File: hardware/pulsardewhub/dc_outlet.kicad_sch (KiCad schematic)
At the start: 18 parts, among them J101 5A DC / center +, U101 TPS26631PWP

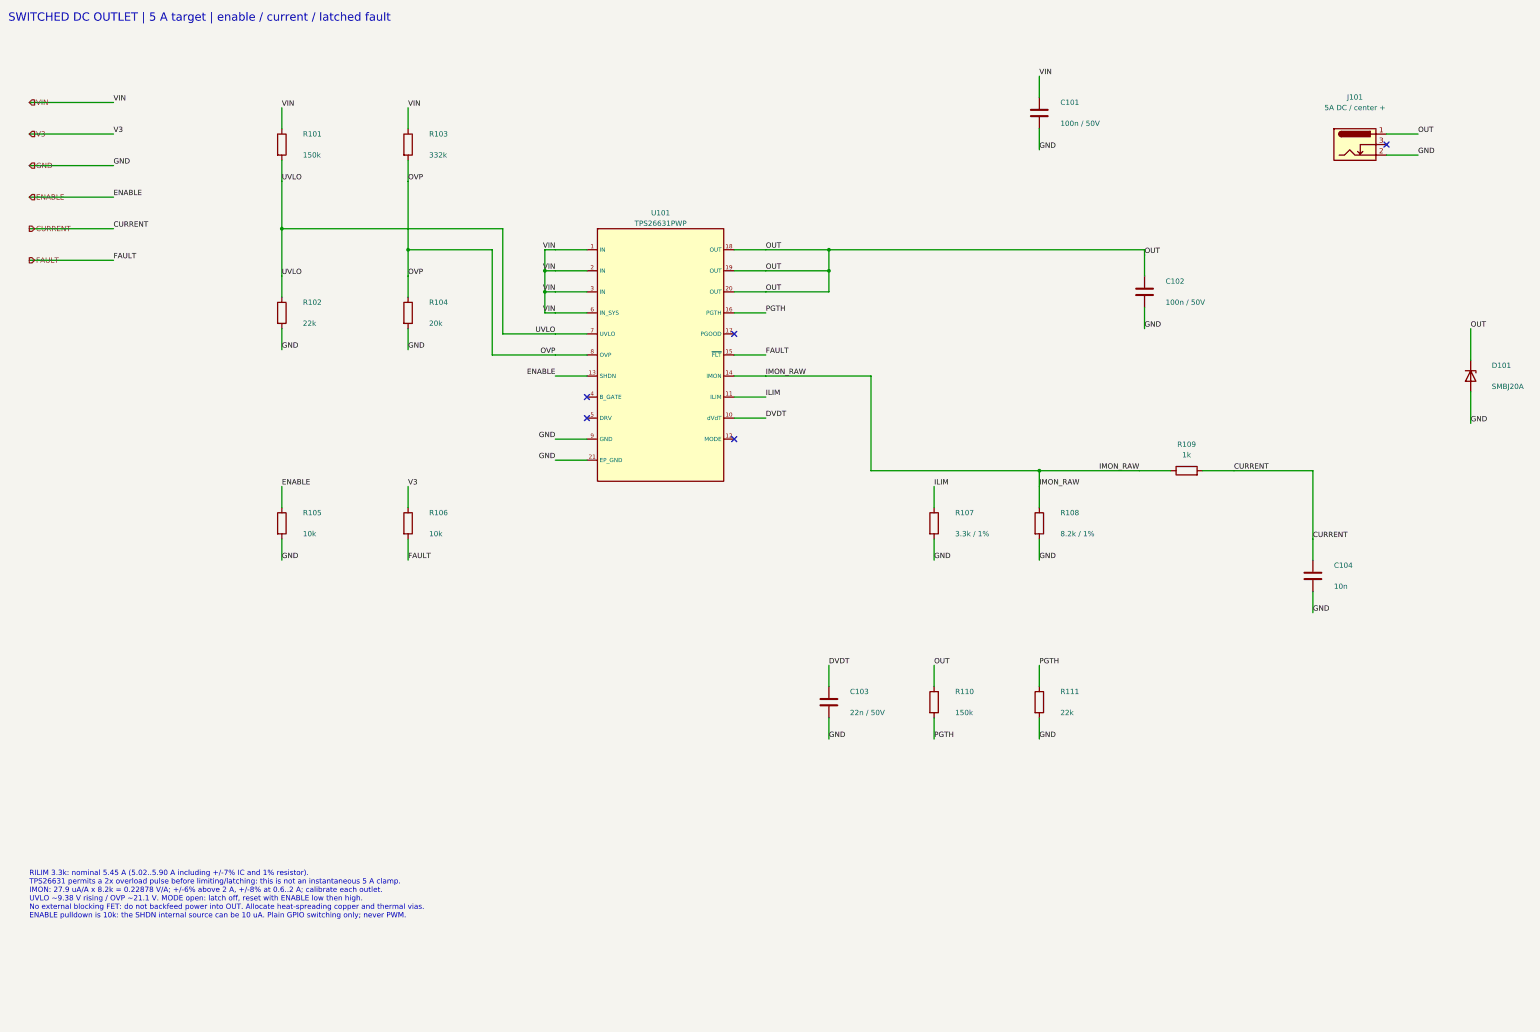
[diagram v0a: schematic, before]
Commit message: Use TPS259827 high-side switches for 12–18 V DC outlets
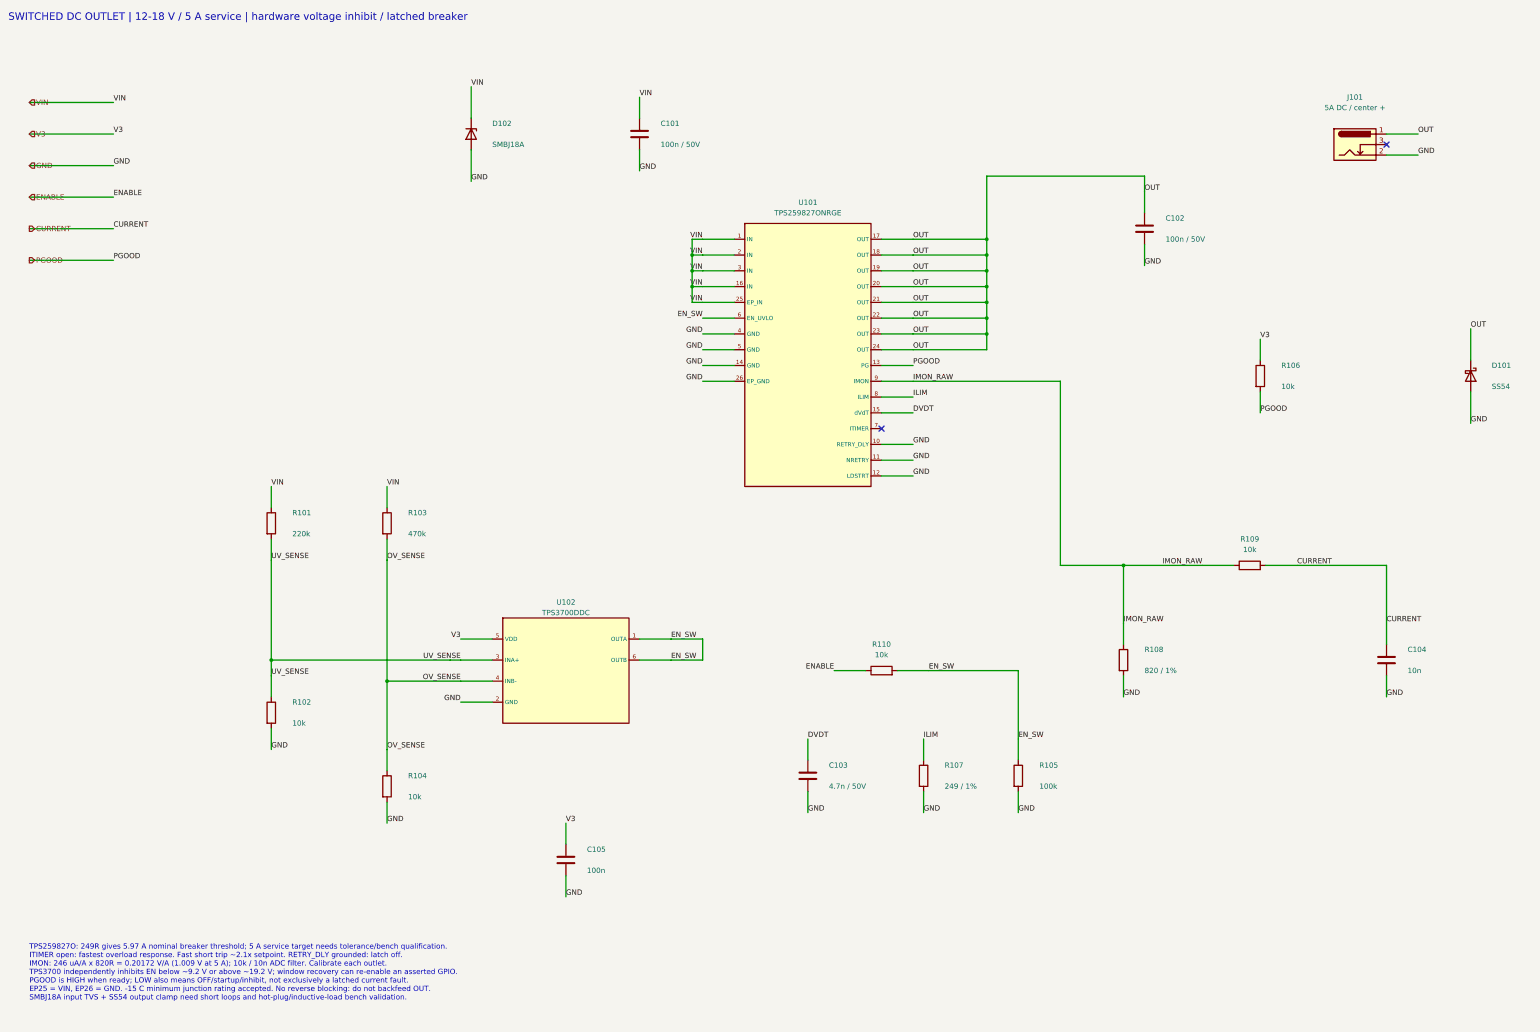
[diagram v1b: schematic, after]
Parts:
- removed R111: 22k, Resistor_SMD:R_0603_1608Metric, symbol Device:R
- added C105: 100n, Capacitor_SMD:C_0603_1608Metric, symbol Device:C
- added D102: SMBJ18A, Diode_SMD:D_SMB, symbol Device:D_Zener
- added U102: TPS3700DDC, Package_TO_SOT_SMD:SOT-23-6, symbol pulsarfab_hub:TPS3700DDC
- C103: value 22n / 50V -> 4.7n / 50V; LCSC C21122 -> C1621; MPN CL10B223KB8NNNC -> CL10B472KB8NNNC
- D101: value SMBJ20A -> SS54; footprint Diode_SMD:D_SMB -> Diode_SMD:D_SMA; symbol Device:D_Zener -> Device:D_Schottky; LCSC C364296 -> C22452; MPN SMBJ20A -> SS54
- R101: value 150k -> 220k; LCSC C22807 -> C22961; MPN 0603WAF1503T5E -> 0603WAF2203T5E
- R102: value 22k -> 10k; LCSC C31850 -> C25804; MPN 0603WAF2202T5E -> 0603WAF1002T5E
- R103: value 332k -> 470k; LCSC C23139 -> C23178; MPN 0603WAF3323T5E -> 0603WAF4703T5E
- R104: value 20k -> 10k; LCSC C4184 -> C25804; MPN 0603WAF2002T5E -> 0603WAF1002T5E
- R105: value 10k -> 100k; LCSC C25804 -> C25803; MPN 0603WAF1002T5E -> 0603WAF1003T5E
- R107: value 3.3k / 1% -> 249 / 1%; LCSC C22978 -> C22919; MPN 0603WAF3301T5E -> 0603WAF2490T5E
- R108: value 8.2k / 1% -> 820 / 1%; LCSC C25981 -> C23253; MPN 0603WAF8201T5E -> 0603WAF8200T5E
- R109: value 1k -> 10k; LCSC C21190 -> C25804; MPN 0603WAF1001T5E -> 0603WAF1002T5E
- R110: value 150k -> 10k; LCSC C22807 -> C25804; MPN 0603WAF1503T5E -> 0603WAF1002T5E
- U101: value TPS26631PWP -> TPS259827ONRGE; footprint pulsarfab:TI_PWP0020T_EP2.96x2.96mm -> pulsarfab:TI_RGE0024M_VQFN24_2EP_4x4mm; symbol pulsarfab_hub:TPS26631PWP -> pulsarfab_hub:TPS259827ONRGE; LCSC C2866319 -> C2155765; MPN TPS26631PWPR -> TPS259827ONRGET
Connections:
- net DVDT: now also U101.15 (dVdT); no longer U101.10 (dVdT)
- net ENABLE: now also R110.1; no longer R105.1, U101.13 (SHDN)
- net GND: now also U101.10 (RETRY_DLY), U101.11 (NRETRY), U101.12 (LDSTRT), U101.14 (GND), U101.26 (EP_GND), U101.4 (GND), U101.5 (GND), C105.2, D102.2 (A), U102.2 (GND); no longer U101.21 (EP_GND), U101.9 (GND)
- net ILIM: now also U101.8 (ILIM); no longer U101.11 (ILIM)
- net IMON_RAW: now also U101.9 (IMON); no longer U101.14 (IMON)
- net OUT: now also U101.17 (OUT), U101.21 (OUT), U101.22 (OUT), U101.23 (OUT), U101.24 (OUT); no longer R110.1
- net V3: now also C105.1, U102.5 (VDD)
- net VIN: now also U101.16 (IN), U101.25 (EP_IN), D102.1 (K); no longer U101.6 (IN_SYS)
- net FAULT renamed PGOOD
- net PGOOD: now also U101.13 (PG); no longer U101.15 (~{FLT})
- net OVP renamed OV_SENSE
- net OV_SENSE: now also U102.4 (INB-); no longer U101.8 (OVP)
- net PGTH renamed EN_SW
- net EN_SW: now also R105.1, U101.6 (EN_UVLO), U102.1 (OUTA), U102.6 (OUTB); no longer U101.16 (PGTH)
- net UVLO renamed UV_SENSE
- net UV_SENSE: now also U102.3 (INA+); no longer U101.7 (UVLO)
- no-connect marks 5 -> 2
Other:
- note added: "SWITCHED DC OUTLET | 12-18 V / 5 A service | hardware voltage inhibit / latched breaker"
- note added: "TPS259827O: 249R gives 5.97 A nominal breaker threshold; 5 A service target needs tolerance/bench qualification. ITIMER open: fastest overload response. Fast short trip ~2.1x setpoint. RETRY_DLY grounded: latch off. IMON: 246 uA/A x 820R = 0.20172 V/A (1.009 V at 5 A); 10k / 10n ADC filter. Calibrate each outlet. TPS3700 independently inhibits EN below ~9.2 V or above ~19.2 V; window recovery can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"
- note removed: "RILIM 3.3k: nominal 5.45 A (5.02..5.90 A including +/-7% IC and 1% resistor). TPS26631 permits a 2x overload pulse before limiting/latching: this is not an instantaneous 5 A clamp. IMON: 27.9 uA/A x 8.2k = 0.22878 V/A; +/-6% above 2 A, +/-8% at 0.6..2 A; calibrate each outlet. UVLO ~9.38 V rising / OVP ~21.1 V. MODE open: latch off, reset with ENABLE low then high. No external blocking FET: do no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"
- note removed: "SWITCHED DC OUTLET | 5 A target | enable / current / latched fault"
- moved on the sheet: C101, C102, C103, C104, R101, R102, R103, R104, R105, R106, R107, R108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

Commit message: Reduce PulsarPower power-path cost while retaining current monitoring
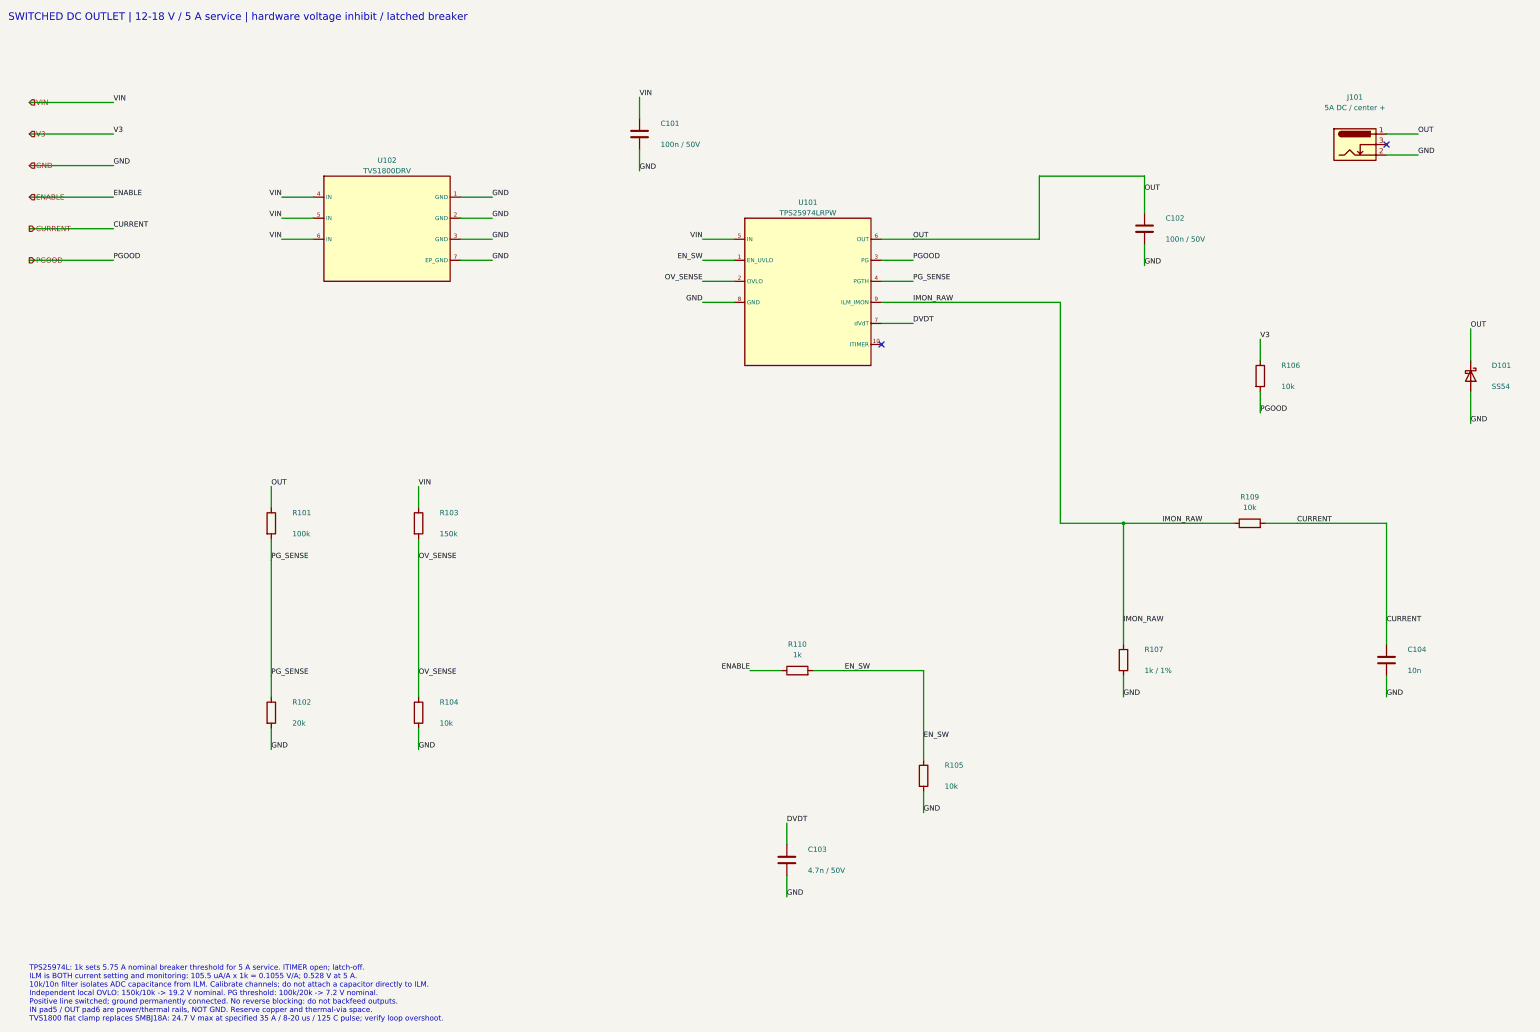
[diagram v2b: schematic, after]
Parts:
- removed C105: 100n, Capacitor_SMD:C_0603_1608Metric, symbol Device:C
- removed D102: SMBJ18A, Diode_SMD:D_SMB, symbol Device:D_Zener
- removed R108: 820 / 1%, Resistor_SMD:R_0603_1608Metric, symbol Device:R
- R101: value 220k -> 100k; LCSC C22961 -> C25803; MPN 0603WAF2203T5E -> 0603WAF1003T5E
- R102: value 10k -> 20k; LCSC C25804 -> C4184; MPN 0603WAF1002T5E -> 0603WAF2002T5E
- R103: value 470k -> 150k; LCSC C23178 -> C22807; MPN 0603WAF4703T5E -> 0603WAF1503T5E
- R105: value 100k -> 10k; LCSC C25803 -> C25804; MPN 0603WAF1003T5E -> 0603WAF1002T5E
- R107: value 249 / 1% -> 1k / 1%; LCSC C22919 -> C21190; MPN 0603WAF2490T5E -> 0603WAF1001T5E
- R110: value 10k -> 1k; LCSC C25804 -> C21190; MPN 0603WAF1002T5E -> 0603WAF1001T5E
- U101: value TPS259827ONRGE -> TPS25974LRPW; footprint pulsarfab:TI_RGE0024M_VQFN24_2EP_4x4mm -> pulsarfab:TI_RPW0010A_VQFN10_2x2mm; symbol pulsarfab_hub:TPS259827ONRGE -> pulsarfab_hub:TPS25974LRPW; LCSC C2155765 -> C3662931; MPN TPS259827ONRGET -> TPS25974LRPWR; Manufacturer TI -> Texas Instruments
- U102: value TPS3700DDC -> TVS1800DRV; footprint Package_TO_SOT_SMD:SOT-23-6 -> Package_SON:WSON-6-1EP_2x2mm_P0.65mm_EP1x1.6mm; symbol pulsarfab_hub:TPS3700DDC -> pulsarfab_hub:TVS1800DRV; LCSC C33002 -> C2649846; MPN TPS3700DDCR -> TVS1800DRVR; Manufacturer TI -> Texas Instruments
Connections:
- net DVDT: now also U101.7 (dVdT); no longer U101.15 (dVdT)
- net EN_SW: now also U101.1 (EN_UVLO); no longer U101.6 (EN_UVLO), U102.1 (OUTA), U102.6 (OUTB)
- net GND: now also U101.8 (GND), U102.1 (GND), U102.3 (GND), U102.7 (EP_GND); no longer U101.10 (RETRY_DLY), U101.11 (NRETRY), U101.12 (LDSTRT), U101.14 (GND), U101.26 (EP_GND), U101.4 (GND), U101.5 (GND)
- net IMON_RAW: now also R107.1
- net OUT: now also R101.1, U101.6 (OUT); no longer U101.17 (OUT), U101.18 (OUT), U101.19 (OUT), U101.20 (OUT), U101.21 (OUT), U101.22 (OUT), U101.23 (OUT), U101.24 (OUT)
- net OV_SENSE: now also U101.2 (OVLO); no longer U102.4 (INB-)
- net PGOOD: now also U101.3 (PG); no longer U101.13 (PG)
- net V3: no longer U102.5 (VDD)
- net VIN: now also U101.5 (IN), U102.4 (IN), U102.5 (IN), U102.6 (IN); no longer R101.1, U101.1 (IN), U101.16 (IN), U101.2 (IN), U101.25 (EP_IN), U101.3 (IN)
- removed net ILIM: R107.1, U101.8 (ILIM)
- net UV_SENSE renamed PG_SENSE
- net PG_SENSE: now also U101.4 (PGTH); no longer U102.3 (INA+)
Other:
- note added: "TPS25974L: 1k sets 5.75 A nominal breaker threshold for 5 A service. ITIMER open; latch-off. ILM is BOTH current setting and monitoring: 105.5 uA/A x 1k = 0.1055 V/A; 0.528 V at 5 A. 10k/10n filter isolates ADC capacitance from ILM. Calibrate channels; do not attach a capacitor directly to ILM. Independent local OVLO: 150k/10k -> 19.2 V nominal. PG threshold: 100k/20k -> 7.2 V nominal. Positive l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"
- note removed: "TPS259827O: 249R gives 5.97 A nominal breaker threshold; 5 A service target needs tolerance/bench qualification. ITIMER open: fastest overload response. Fast short trip ~2.1x setpoint. RETRY_DLY grounded: latch off. IMON: 246 uA/A x 820R = 0.20172 V/A (1.009 V at 5 A); 10k / 10n ADC filter. Calibrate each outlet. TPS3700 independently inhibits EN below ~9.2 V or above ~19.2 V; window recovery can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"
- title: PulsarDew Hub - 5 A switched DC outlet -> PulsarPower - 5 A switched DC outlet
- moved on the sheet: C103, R103, R104, R105, R107, R109, R110

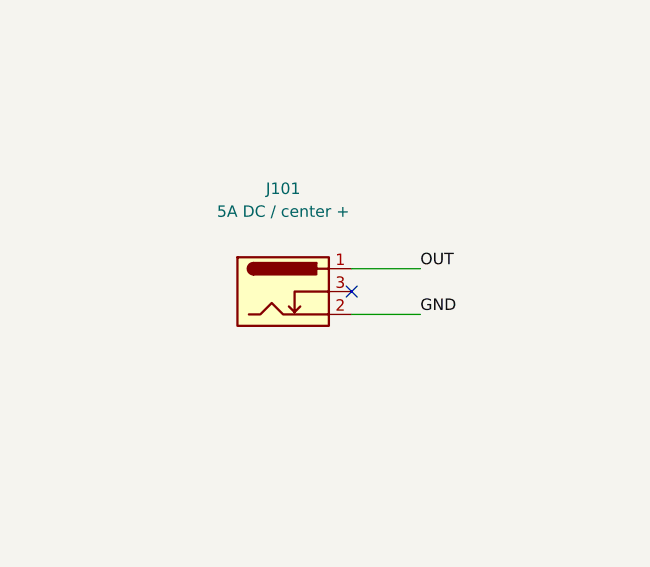
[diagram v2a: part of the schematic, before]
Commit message: Use owned XKB barrel sockets and evaluate LMR51610 commonality
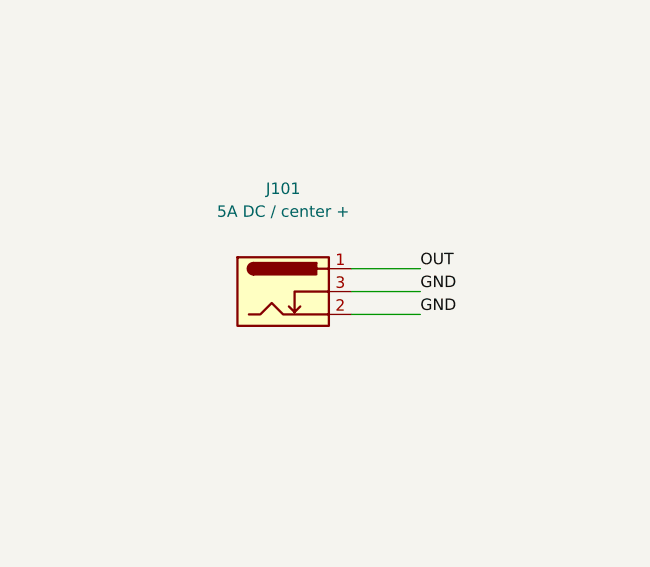
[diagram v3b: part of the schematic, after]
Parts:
- J101: footprint pulsarfab:BarrelJack_GCT_DCJ200_Edge -> pulsarfab:BarrelJack_XKB_DC-005K-5A_Edge; LCSC C5280493 -> C2880546; MPN DCJ200-10-A-K1-K -> DC-005K-5A-2.0; Manufacturer Global Connector Technology -> XKB Connection
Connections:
- net GND: now also J101.3
- no-connect marks 2 -> 1
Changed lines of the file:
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@@
       (font
         (size 1.27 1.27))))
-  (property "Footprint" "pulsarfab:BarrelJack_GCT_DCJ200_Edge"
-    (at 345.44 48.26 0.0)
-    (effects
-      (font
-        (size 1.27 1.27))
-      (hide yes)))
-  (property "Datasheet" "https://datasheet.lcsc.com/datasheet/pdf/9e28732f65d9d59bee76802895b2add9.pdf?productCode=C5280493"
-    (at 345.44 48.26 0.0)
-    (effects
-      (font
-        (size 1.27 1.27))
-      (hide yes)))
-  (property "LCSC" "C5280493"
-    (at 345.44 48.26 0.0)
-    (effects
-      (font
-        (size 1.27 1.27))
-      (hide yes)))
-  (property "MPN" "DCJ200-10-A-K1-K"
-    (at 345.44 48.26 0.0)
-    (effects
-      (font
-        (size 1.27 1.27))
-      (hide yes)))
-  (property "Manufacturer" "Global Connector Technology"
+  (property "Footprint" "pulsarfab:BarrelJack_XKB_DC-005K-5A_Edge"
+    (at 345.44 48.26 0.0)
+    (effects
+      (font
+        (size 1.27 1.27))
+      (hide yes)))
+  (property "Datasheet" "https://datasheet.lcsc.com/datasheet/pdf/42a925a8542473f46554cf6f67b6cc91.pdf?productCode=C2880546"
+    (at 345.44 48.26 0.0)
+    (effects
+      (font
+        (size 1.27 1.27))
+      (hide yes)))
+  (property "LCSC" "C2880546"
+    (at 345.44 48.26 0.0)
+    (effects
+      (font
+        (size 1.27 1.27))
+      (hide yes)))
+  (property "MPN" "DC-005K-5A-2.0"
+    (at 345.44 48.26 0.0)
+    (effects
+      (font
+        (size 1.27 1.27))
+      (hide yes)))
+  (property "Manufacturer" "XKB Connection"
     (at 345.44 48.26 0.0)
     (effects
@@
 (label "OUT"  (at 360.6800 45.7200 0) (effects (font (size 1.27 1.27)) (justify left bottom)))
 (label "GND"  (at 360.6800 50.8000 0) (effects (font (size 1.27 1.27)) (justify left bottom)))
-(no_connect (at 353.0600 48.2600))
+(label "GND"  (at 360.6800 48.2600 0) (effects (font (size 1.27 1.27)) (justify left bottom)))
 (symbol
   (lib_id "Device:D_Schottky")
@@
 (wire (pts (xy 331.4700 139.7000) (xy 353.0600 139.7000)) (stroke (width 0) (type default)))
 (wire (pts (xy 353.0600 45.7200) (xy 360.6800 45.7200)) (stroke (width 0) (type default)))
+(wire (pts (xy 353.0600 48.2600) (xy 360.6800 48.2600)) (stroke (width 0) (type default)))
 (wire (pts (xy 353.0600 50.8000) (xy 360.6800 50.8000)) (stroke (width 0) (type default)))
 (wire (pts (xy 353.0600 139.7000) (xy 353.0600 163.8300)) (stroke (width 0) (type default)))
